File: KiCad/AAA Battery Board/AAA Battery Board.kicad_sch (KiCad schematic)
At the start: 4 parts, among them J1 To Mobo

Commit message: Add zip tie holes
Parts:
- D1: value 1N5817 -> 1N4148; footprint Diode_THT:D_DO-41_SOD81_P7.62mm_Horizontal -> Diode_THT:D_DO-35_SOD27_P7.62mm_Horizontal
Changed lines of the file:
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@@
       (effects (font (size 1.27 1.27)) (justify right))
     )
-    (property "Value" "1N5817" (at 160.02 102.87 90)
+    (property "Value" "1N4148" (at 160.02 102.87 90)
       (effects (font (size 1.27 1.27)) (justify right))
     )
-    (property "Footprint" "Diode_THT:D_DO-41_SOD81_P7.62mm_Horizontal" (at 157.48 101.6 0)
+    (property "Footprint" "Diode_THT:D_DO-35_SOD27_P7.62mm_Horizontal" (at 157.48 101.6 0)
       (effects (font (size 1.27 1.27)) hide)
     )

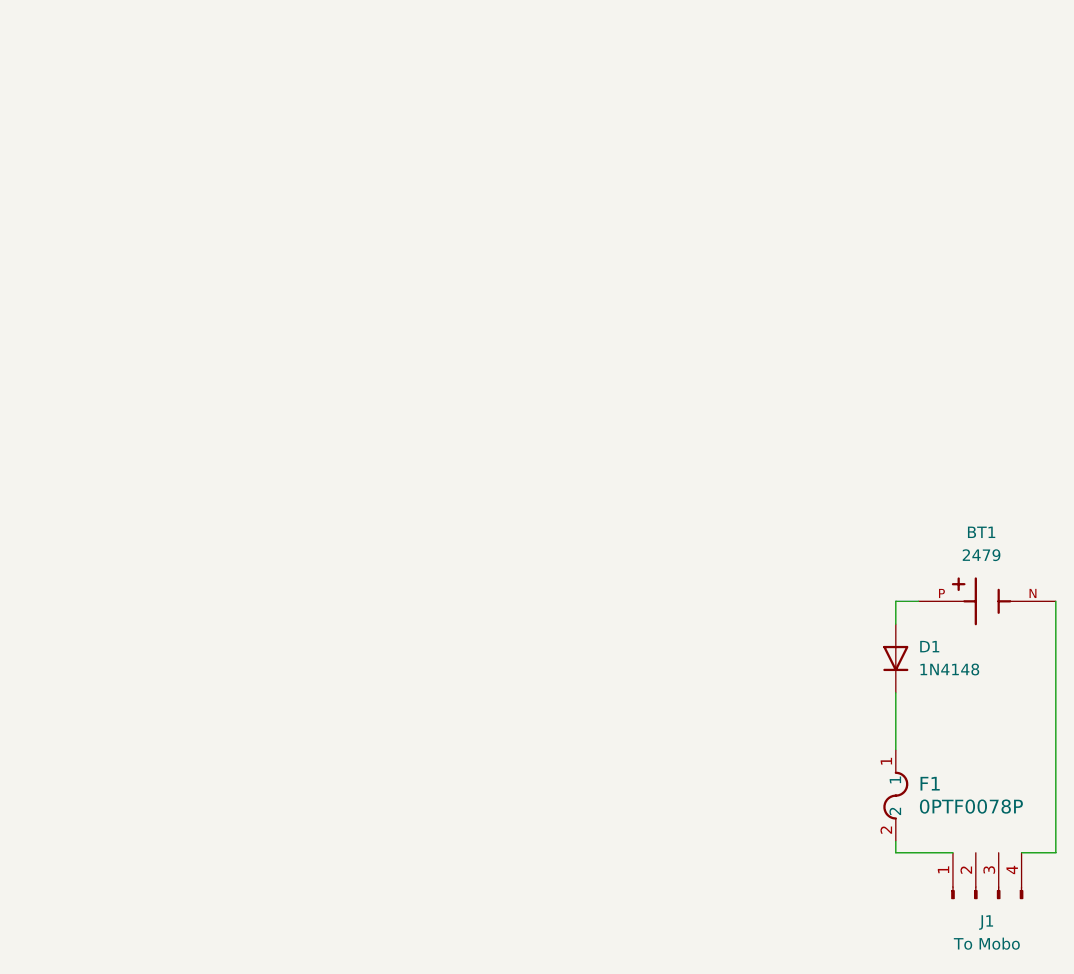
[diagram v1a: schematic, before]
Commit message: Update footprints.
Update fuse holder footprint to work with both 15mm and 23mm leg spacing versions.
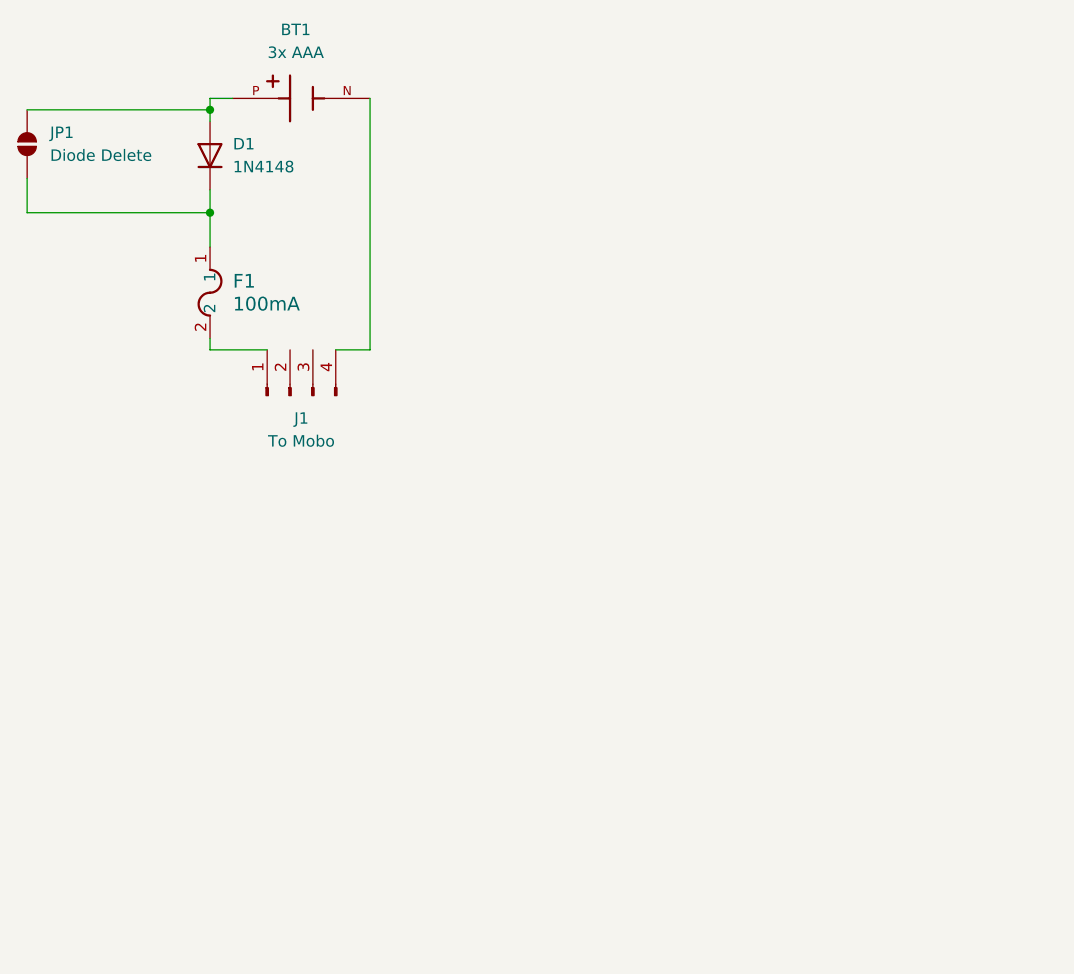
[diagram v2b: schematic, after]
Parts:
- added JP1: Diode Delete, Jumper:SolderJumper-2_P1.3mm_Open_TrianglePad1.0x1.5mm, symbol Jumper:SolderJumper_2_Open
- BT1: value 2479 -> 3x AAA
- F1: value 0PTF0078P -> 100mA; footprint FUSE_0PTF0078P_LTF -> PCRestoLib:UniversalGreenFuseHolder
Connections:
- net at BT1.P, D1.2 (A): now also JP1.1 (A)
- net at D1.1 (K), F1.1: now also JP1.2 (B)
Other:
- moved on the sheet: BT1, D1, F1, J1
